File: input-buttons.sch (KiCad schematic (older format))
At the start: 52 parts

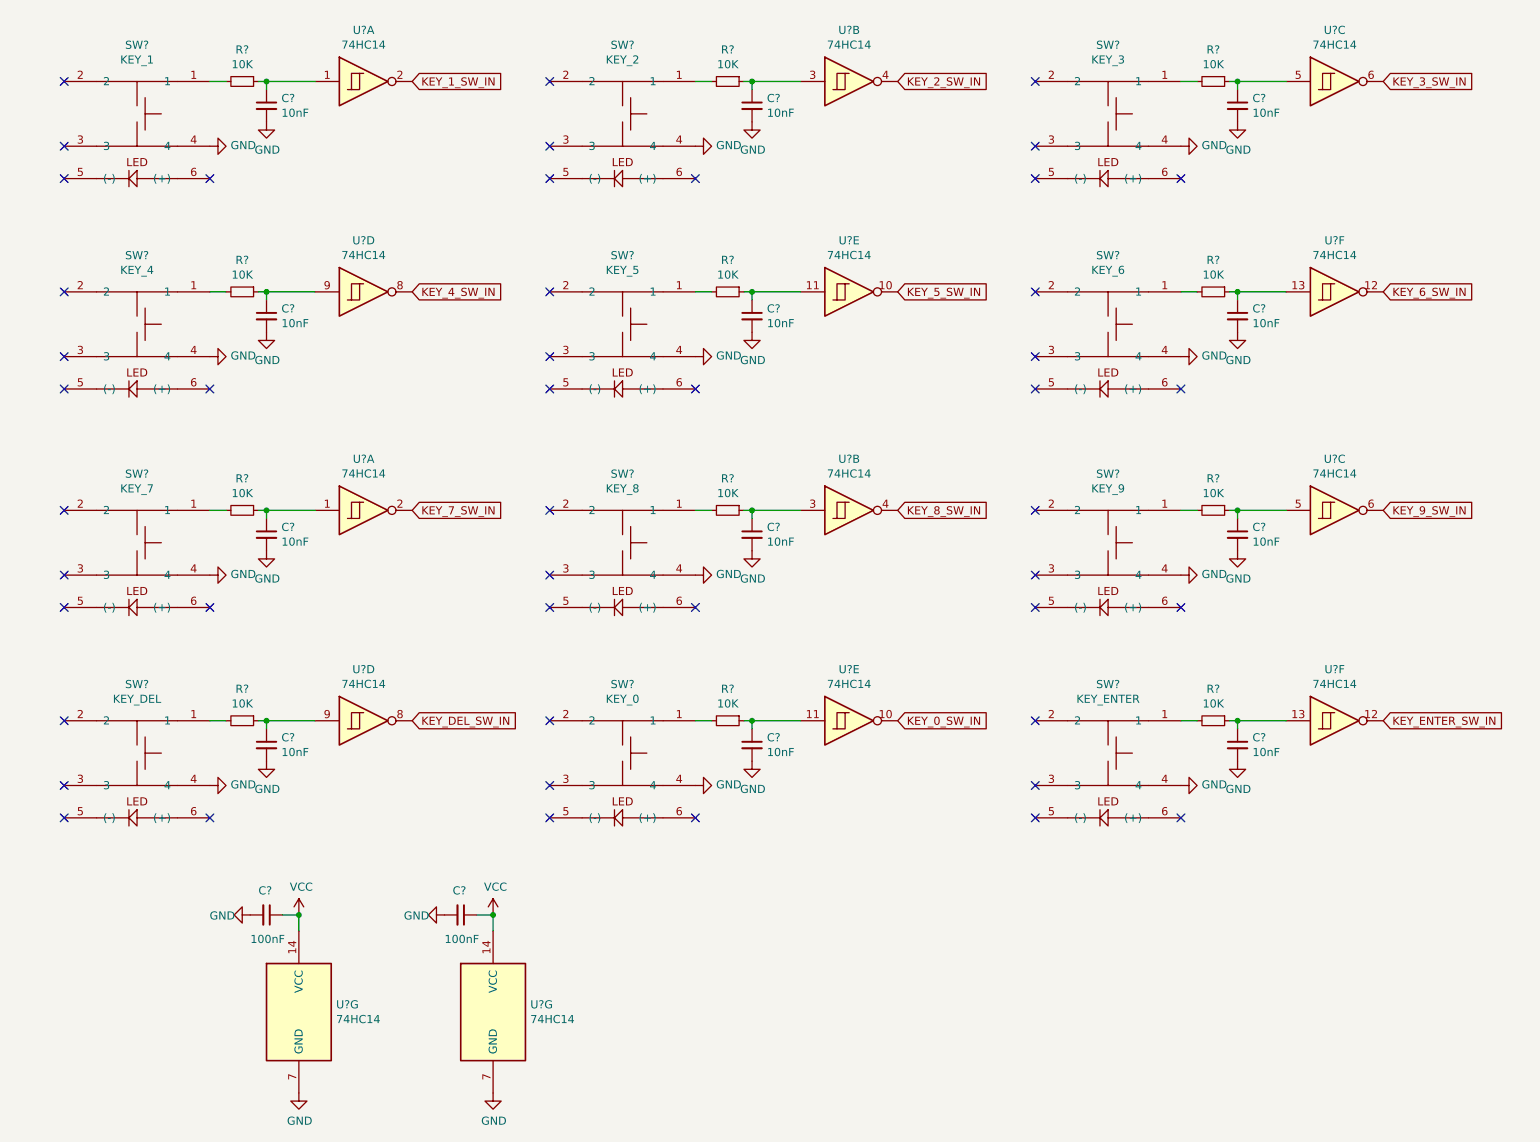
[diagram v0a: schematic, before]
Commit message: Initial PCB routed
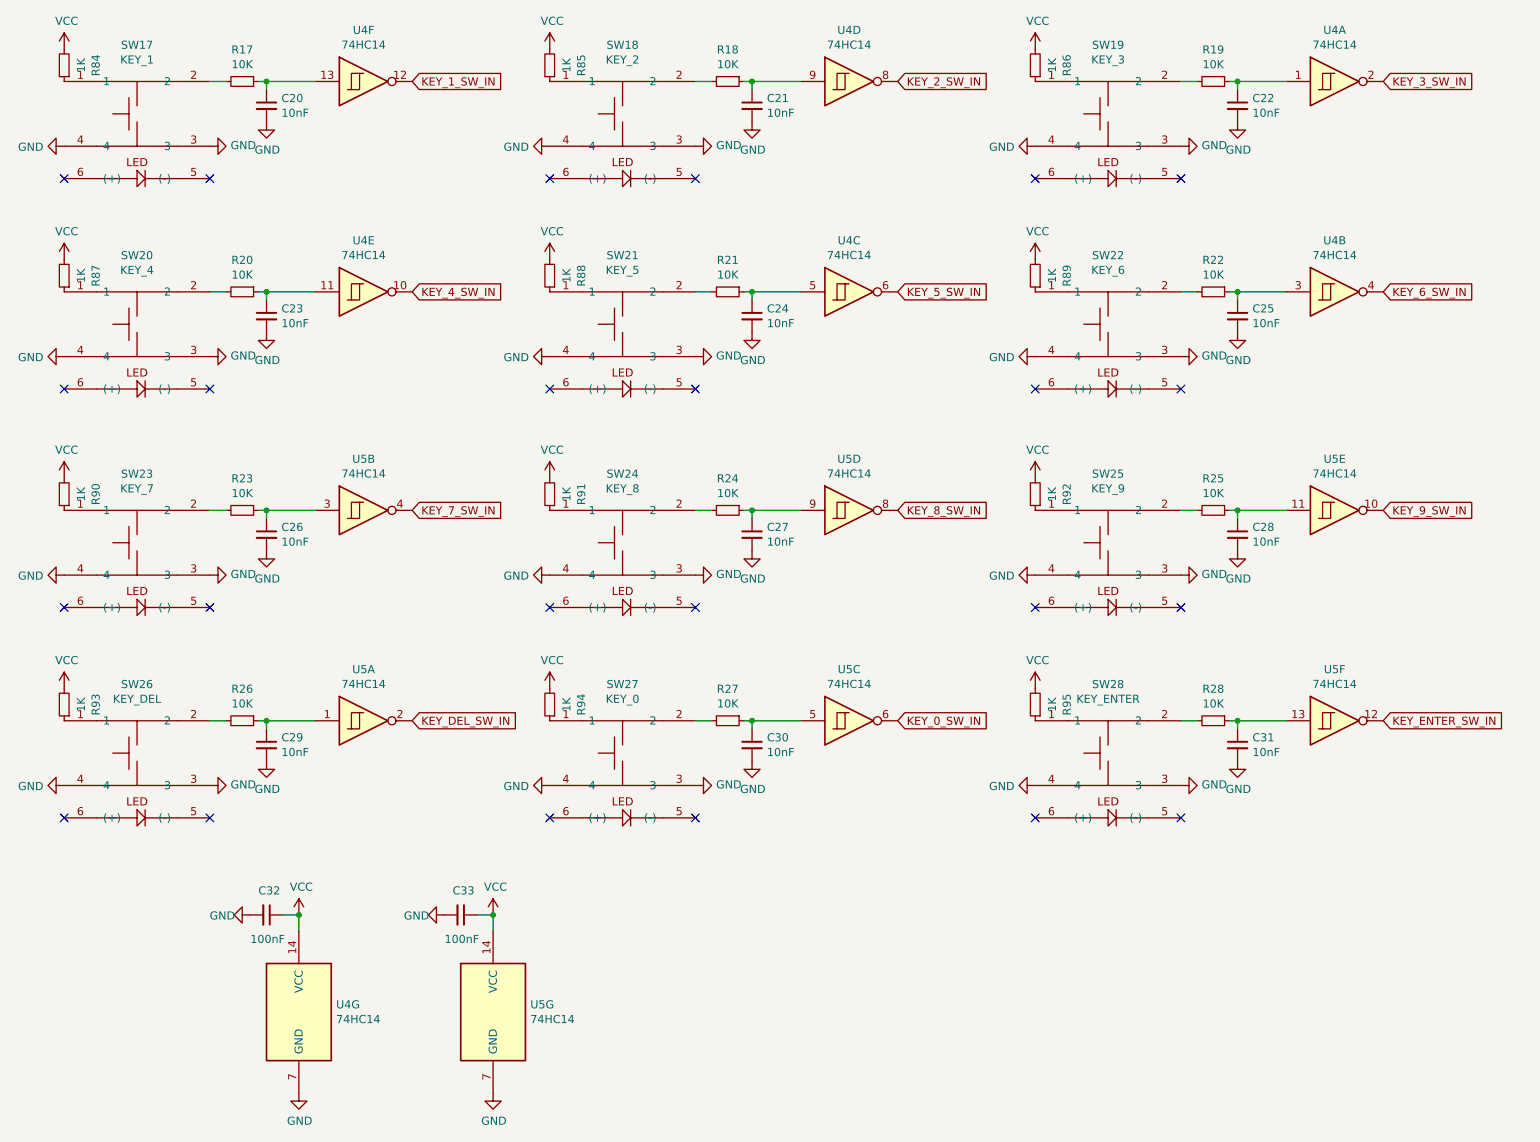
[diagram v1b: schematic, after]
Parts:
- added R84, R85, R86, R87, R88, R89, R90, R91, R92, R93, R94, R95: 1K, Resistor_SMD:R_0603_1608Metric_Pad0.98x0.95mm_HandSolder, symbol Device:R_Small
- C20, C21, C22, C23, C24, C25, C26, C27, C28, C29, C30, C31, C32, C33: renamed from C?; footprint (none) -> Capacitor_SMD:C_0603_1608Metric_Pad1.08x0.95mm_HandSolder
- R17, R18, R19, R20, R21, R22, R23, R24, R25, R26, R27, R28: renamed from R?; footprint (none) -> Resistor_SMD:R_0603_1608Metric_Pad0.98x0.95mm_HandSolder
- SW17, SW18, SW19, SW20, SW21, SW22, SW23, SW24, SW25, SW26, SW27, SW28: renamed from SW?; footprint (none) -> TL-1240:TL-1240
- U4, U5: renamed from U?; footprint (none) -> Package_SO:SSOP-14_5.3x6.2mm_P0.65mm
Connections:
- net GND: now also SW17.3, SW18.3, SW19.3, SW20.3, SW21.3, SW22.3, SW23.3, SW24.3, SW25.3, SW26.3, SW27.3, SW28.3
- net KEY_0_SW_IN: now also U5.6; no longer U5.10
- net KEY_1_SW_IN: now also U4.12; no longer U4.2
- net KEY_2_SW_IN: now also U4.8; no longer U4.4
- net KEY_3_SW_IN: now also U4.2; no longer U4.6
- net KEY_4_SW_IN: now also U4.10; no longer U4.8
- net KEY_5_SW_IN: now also U4.6; no longer U4.10
- net KEY_6_SW_IN: now also U4.4; no longer U4.12
- net KEY_7_SW_IN: now also U5.4; no longer U5.2
- net KEY_8_SW_IN: now also U5.8; no longer U5.4
- net KEY_9_SW_IN: now also U5.10; no longer U5.6
- net KEY_DEL_SW_IN: now also U5.2; no longer U5.8
- net VCC: now also R84.2, R85.2, R86.2, R87.2, R88.2, R89.2, R90.2, R91.2, R92.2, R93.2, R94.2, R95.2
- net at SW17.1: now also R84.1; no longer R17.2
- net at SW17.2: now also R17.2
- net at C20.1, R17.1: now also U4.13; no longer U4.1
- net at SW18.1: now also R85.1; no longer R18.2
- net at SW18.2: now also R18.2
- net at C21.1, R18.1: now also U4.9; no longer U4.3
- net at SW19.1: now also R86.1; no longer R19.2
- net at SW19.2: now also R19.2
- net at C22.1, R19.1: now also U4.1; no longer U4.5
- net at SW20.1: now also R87.1; no longer R20.2
- net at SW20.2: now also R20.2
- net at C23.1, R20.1: now also U4.11; no longer U4.9
- net at SW21.1: now also R88.1; no longer R21.2
- net at SW21.2: now also R21.2
- net at C24.1, R21.1: now also U4.5; no longer U4.11
- net at SW22.1: now also R89.1; no longer R22.2
- net at SW22.2: now also R22.2
- net at C25.1, R22.1: now also U4.3; no longer U4.13
- net at SW23.1: now also R90.1; no longer R23.2
- net at SW23.2: now also R23.2
- net at C26.1, R23.1: now also U5.3; no longer U5.1
- net at SW24.1: now also R91.1; no longer R24.2
- net at SW24.2: now also R24.2
- net at C27.1, R24.1: now also U5.9; no longer U5.3
- net at SW25.1: now also R92.1; no longer R25.2
- net at SW25.2: now also R25.2
- net at C28.1, R25.1: now also U5.11; no longer U5.5
- net at SW26.1: now also R93.1; no longer R26.2
- net at SW26.2: now also R26.2
- net at C29.1, R26.1: now also U5.1; no longer U5.9
- net at SW27.1: now also R94.1; no longer R27.2
- net at SW27.2: now also R27.2
- net at C30.1, R27.1: now also U5.5; no longer U5.11
- net at SW28.1: now also R95.1; no longer R28.2
- net at SW28.2: now also R28.2
- no-connect marks 48 -> 24
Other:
- moved on the sheet: U4A, U4B, U4C, U4D, U4E, U4F, U5A, U5B, U5C, U5D, U5E

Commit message: Initial revision B
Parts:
- SW17, SW18, SW19, SW20, SW21, SW22, SW23, SW24, SW25, SW26, SW27, SW28: footprint TL-1240:TL-1240 -> TL-1265:TL-1265_NO_LED; symbol e-switch-tact:TL-1240 -> e-switch-tact:TL-1240-NO_LED
- U4, U5: footprint Package_SO:SSOP-14_5.3x6.2mm_P0.65mm -> Package_SO:TSSOP-14_4.4x5mm_P0.65mm
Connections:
- no-connect marks 24 -> 0
